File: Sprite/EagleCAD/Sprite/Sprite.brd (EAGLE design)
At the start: 35 x 35 mm, 32 parts, among them P1 SPRITE_PIN, P2 SPRITE_PIN, U1 CC430F5137, U2 HMC5883LSMD, U3 ITG-3200

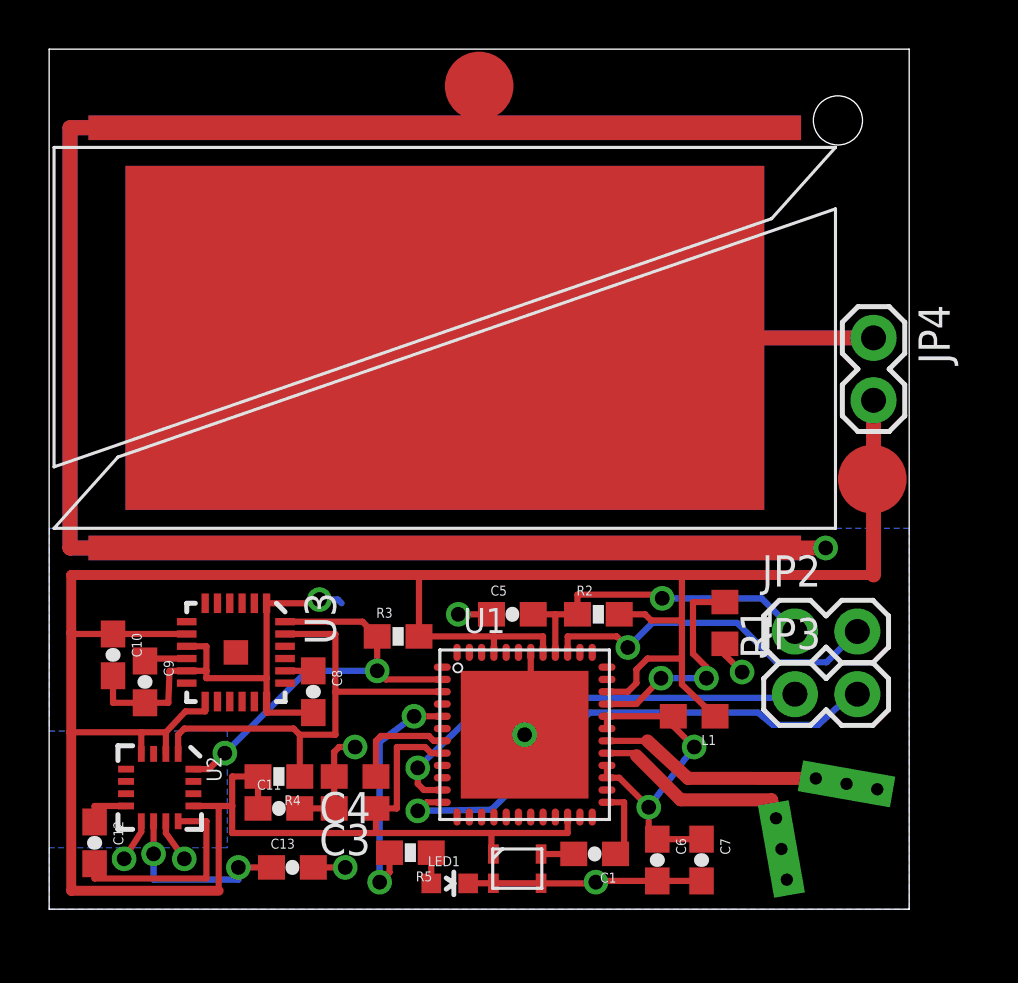
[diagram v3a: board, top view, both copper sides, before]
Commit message: Made corner hole 2.8 mm
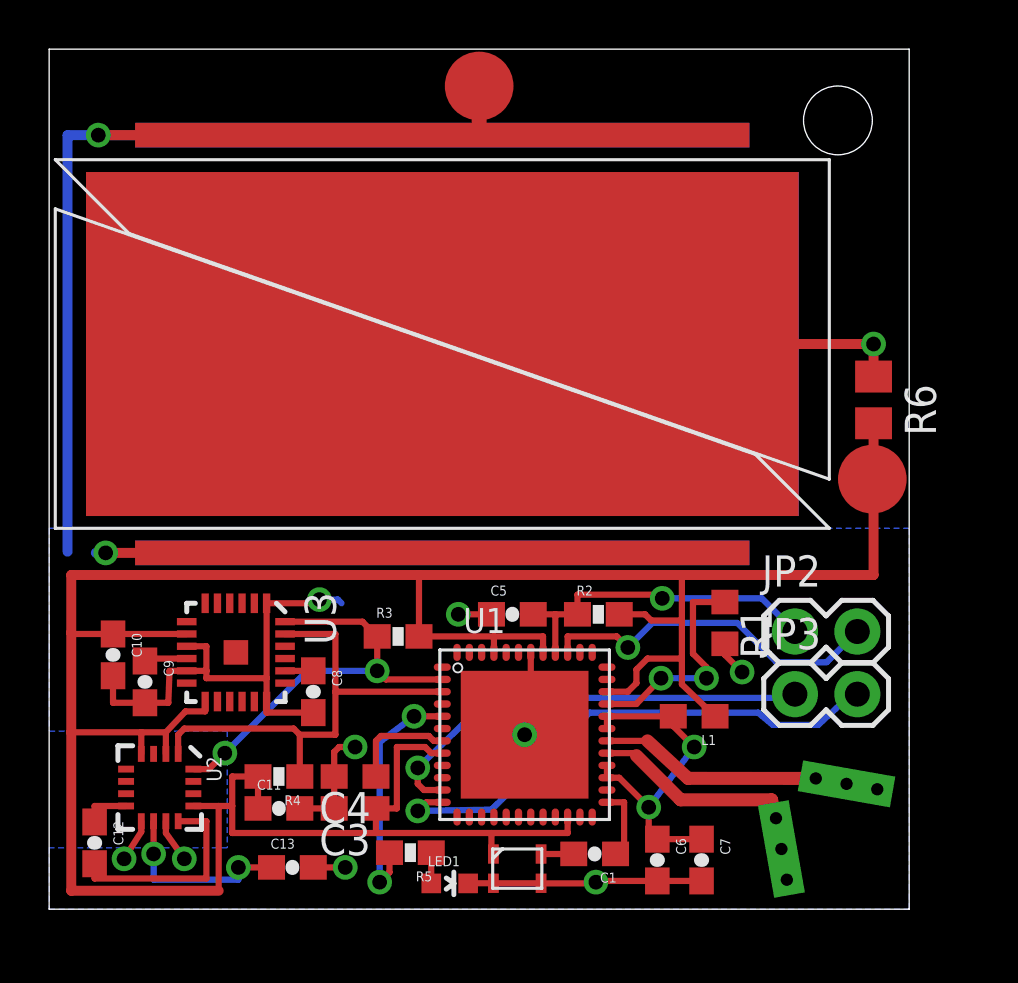
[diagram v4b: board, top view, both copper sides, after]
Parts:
- removed JP4: (no value), SparkFun:1X02
- added R6: 0, rcl:R0805
- moved S2 17.7 mm to (16.0, 23.0)
- moved S1 17.5 mm to (16.0, 23.0)
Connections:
- net VCC: now also R6.2; no longer JP4.2
- net VSOLAR: now also R6.1; no longer JP4.1
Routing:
- net GND: track 156.2 -> 109.3 mm, vias 10 -> 11
- net VSOLAR: track 34.9 -> 36.4 mm, vias 0 -> 1
- net VCC: track 124.2 -> 123.2 mm
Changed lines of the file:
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@@
 <wire x1="35" y1="35" x2="0" y2="35" width="0" layer="20"/>
 <wire x1="0" y1="35" x2="0" y2="0" width="0" layer="20"/>
-<hole x="32.1" y="32.1" drill="2"/>
+<hole x="32.1" y="32.1" drill="2.8"/>
 </plain>
 <attributes>
@@
 <element name="LED1" library="SparkFun" package="LED-0603" value="" x="16.3" y="1.05" rot="R270"/>
 <element name="R5" library="SparkFun" package="0603-RES" value="270R" x="14.7" y="2.3" rot="R180"/>
-<element name="JP4" library="SparkFun" package="1X02" value="" x="33.55" y="23.25" rot="R270"/>
 <element name="JP3" library="SparkFun" package="1X02" value="" x="30.35" y="8.75"/>
-<element name="S2" library="TASC" package="TASC" value="TASC" x="32" y="15.5" rot="MR0"/>
 <element name="U$1" library="SpriteTCXO" package="TXC_7Z" value="TCXO_7Z" x="19.05" y="1.65"/>
 <element name="P2" library="SpritePin" package="SPRITE_PIN" value="SPRITE_PIN" x="17.5" y="33.5"/>
 <element name="P1" library="SpritePin" package="SPRITE_PIN" value="SPRITE_PIN" x="33.5" y="17.5"/>
-<element name="S1" library="TASC" package="TASC" value="TASC" x="0.2" y="15.5"/>
+<element name="S1" library="TASC" package="TASC" value="TASC" x="16" y="23"/>
+<element name="S2" library="TASC" package="TASC" value="TASC" x="16" y="23" rot="MR0"/>
+<element name="R6" library="rcl" package="R0805" value="0" x="33.55" y="20.725" rot="R270"/>
 </elements>
 <signals>
@@
 <wire x1="25.75" y1="9.15" x2="27.1" y2="7.85" width="0.254" layer="1"/>
 <wire x1="24.5" y1="11.75" x2="25.75" y2="11.75" width="0.254" layer="1"/>
-<contactref element="JP4" pad="2"/>
 <contactref element="U$1" pad="VCC"/>
 <wire x1="18.08" y1="2.245" x2="18" y2="2.345" width="0.254" layer="1"/>
 <wire x1="18" y1="2.345" x2="18" y2="3.1" width="0.254" layer="1"/>
-<wire x1="33.55" y1="20.71" x2="33.55" y2="13.6" width="0.6096" layer="1"/>
 <wire x1="25.75" y1="11.75" x2="25.75" y2="13.5" width="0.254" layer="1"/>
 <wire x1="24.5" y1="11.75" x2="24.25" y2="12" width="0.254" layer="1"/>
@@
 <wire x1="6.9" y1="4.2" x2="6.9" y2="0.75" width="0.254" layer="1"/>
 <wire x1="6.9" y1="4.2" x2="5.87" y2="4.2" width="0.254" layer="1"/>
+<contactref element="R6" pad="2"/>
+<wire x1="33.55" y1="19.775" x2="33.55" y2="13.6" width="0.4064" layer="1"/>
 <wire x1="20.1" y1="10.45" x2="22.7" y2="8.85" width="0" layer="19" extent="1-1"/>
 </signal>
@@
 <wire x1="20.02" y1="1.05" x2="20.02" y2="1.055" width="0.254" layer="1"/>
 <wire x1="18.08" y1="1.055" x2="20.02" y2="1.055" width="0.254" layer="1"/>
-<contactref element="S2" pad="MINUS1"/>
-<contactref element="S2" pad="MINUS2"/>
-<contactref element="S1" pad="MINUS2"/>
-<contactref element="S1" pad="MINUS1"/>
-<wire x1="16.1" y1="31.8" x2="0.85" y2="31.8" width="0.6096" layer="16"/>
-<wire x1="0.85" y1="31.8" x2="0.85" y2="14.7" width="0.6096" layer="16"/>
-<wire x1="0.85" y1="14.7" x2="16.1" y2="14.7" width="0.6096" layer="16"/>
-<wire x1="16.1" y1="31.8" x2="0.85" y2="31.8" width="0.6096" layer="1"/>
-<wire x1="0.85" y1="31.8" x2="0.85" y2="14.7" width="0.6096" layer="1"/>
-<wire x1="0.85" y1="14.7" x2="16.1" y2="14.7" width="0.6096" layer="1"/>
 <wire x1="27.5" y1="10.8" x2="27.5" y2="10.35" width="0.254" layer="1"/>
 <wire x1="27.5" y1="10.35" x2="28.2" y2="9.65" width="0.254" layer="1"/>
@@
 <wire x1="10.75" y1="1.7" x2="12.05" y2="1.7" width="0.254" layer="1"/>
 <via x="12.05" y="1.7" extent="1-16" drill="0.6"/>
-<wire x1="16.1" y1="14.7" x2="31.6" y2="14.7" width="0.6096" layer="1"/>
-<via x="31.6" y="14.7" extent="1-16" drill="0.6"/>
-<wire x1="31.6" y1="14.7" x2="31.55" y2="14.7" width="0.6096" layer="16"/>
 <wire x1="20.02" y1="1.05" x2="22.2" y2="1.05" width="0.254" layer="1"/>
 <wire x1="22.2" y1="1.05" x2="22.25" y2="1.1" width="0.254" layer="1"/>
@@
 <vertex x="0" y="2.5"/>
 </polygon>
+<contactref element="S1" pad="MINUS1"/>
+<contactref element="S1" pad="MINUS2"/>
+<contactref element="S2" pad="MINUS1"/>
+<contactref element="S2" pad="MINUS2"/>
+<wire x1="16" y1="31.5" x2="17.5" y2="31.5" width="0.4064" layer="1"/>
+<wire x1="17.5" y1="31.5" x2="17.5" y2="33.5" width="0.6096" layer="1"/>
+<wire x1="16" y1="31.5" x2="2" y2="31.5" width="0.4064" layer="1"/>
+<wire x1="16" y1="14.55" x2="16" y2="14.5" width="0.4064" layer="1"/>
+<wire x1="16" y1="31.5" x2="2" y2="31.5" width="0.4064" layer="16"/>
+<via x="2" y="31.5" extent="1-16" drill="0.6"/>
+<wire x1="2" y1="31.5" x2="0.75" y2="31.5" width="0.4064" layer="16"/>
+<wire x1="0.75" y1="31.5" x2="0.75" y2="14.55" width="0.4064" layer="16"/>
+<wire x1="16" y1="14.5" x2="2.3" y2="14.5" width="0.4064" layer="1"/>
+<via x="2.3" y="14.5" extent="1-16" drill="0.6"/>
+<wire x1="2.3" y1="14.5" x2="1.9" y2="14.5" width="0.4064" layer="16"/>
 </signal>
 <signal name="N$3">
@@
 </signal>
 <signal name="VSOLAR">
-<contactref element="JP4" pad="1"/>
+<contactref element="S1" pad="PLUS"/>
 <contactref element="S2" pad="PLUS"/>
-<contactref element="S1" pad="PLUS"/>
-<wire x1="33.55" y1="23.25" x2="16.1" y2="23.25" width="0.6096" layer="1"/>
-<wire x1="16.1" y1="23.25" x2="33.55" y2="23.25" width="0.6096" layer="16"/>
+<contactref element="R6" pad="1"/>
+<wire x1="16" y1="23" x2="33.55" y2="23" width="0.4064" layer="1"/>
+<wire x1="16" y1="23" x2="33.55" y2="23" width="0.4064" layer="16"/>
+<via x="33.55" y="23" extent="1-16" drill="0.6"/>
+<wire x1="33.55" y1="23" x2="33.55" y2="21.675" width="0.4064" layer="1"/>
 </signal>
 <signal name="TXD">
@@
 </signal>
 </signals>
-<errors>
-</errors>
 </board>
 </drawing>

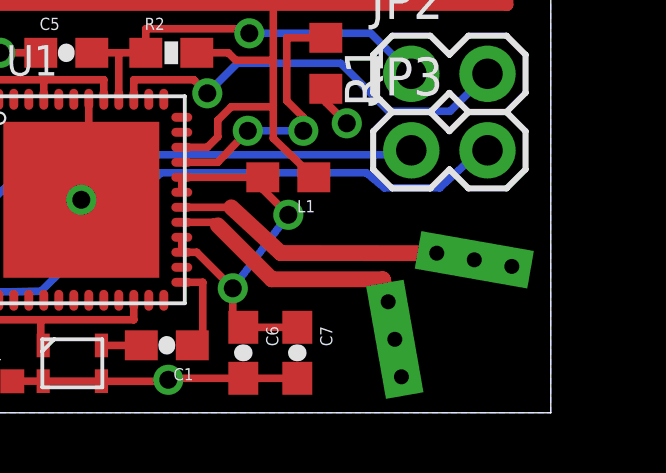
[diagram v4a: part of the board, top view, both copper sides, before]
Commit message: Updated Gerbers and BOM for new Sprite order
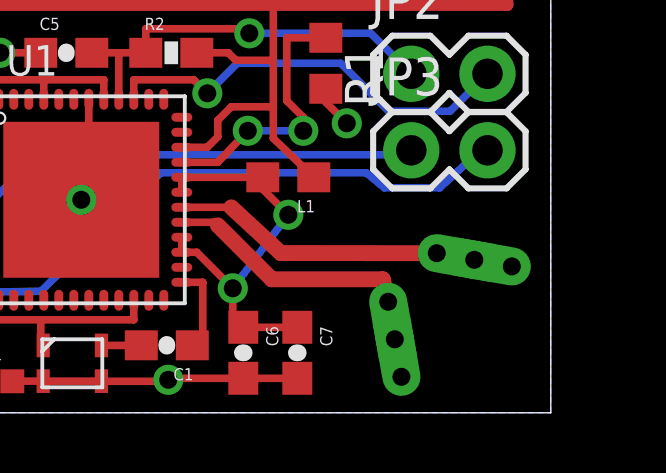
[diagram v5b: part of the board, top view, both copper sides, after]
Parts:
- renumbered U$1 to X1
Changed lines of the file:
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@@
 <element name="R5" library="SparkFun" package="0603-RES" value="270R" x="14.7" y="2.3" rot="R180"/>
 <element name="JP3" library="SparkFun" package="1X02" value="" x="30.35" y="8.75"/>
-<element name="U$1" library="SpriteTCXO" package="TXC_7Z" value="TCXO_7Z" x="19.05" y="1.65"/>
+<element name="X1" library="SpriteTCXO" package="TXC_7Z" value="TCXO_7Z" x="19.05" y="1.65"/>
 <element name="P2" library="SpritePin" package="SPRITE_PIN" value="SPRITE_PIN" x="17.5" y="33.5"/>
 <element name="P1" library="SpritePin" package="SPRITE_PIN" value="SPRITE_PIN" x="33.5" y="17.5"/>
@@
 <wire x1="25.75" y1="9.15" x2="27.1" y2="7.85" width="0.254" layer="1"/>
 <wire x1="24.5" y1="11.75" x2="25.75" y2="11.75" width="0.254" layer="1"/>
-<contactref element="U$1" pad="VCC"/>
+<contactref element="X1" pad="VCC"/>
 <wire x1="18.08" y1="2.245" x2="18" y2="2.345" width="0.254" layer="1"/>
 <wire x1="18" y1="2.345" x2="18" y2="3.1" width="0.254" layer="1"/>
@@
 <wire x1="6.4" y1="9.7" x2="5.6" y2="9.7" width="0.254" layer="1"/>
 <wire x1="6.4" y1="9.7" x2="6.4" y2="9.4" width="0.254" layer="1"/>
-<contactref element="U$1" pad="GND2"/>
-<contactref element="U$1" pad="GND1"/>
+<contactref element="X1" pad="GND2"/>
+<contactref element="X1" pad="GND1"/>
 <wire x1="20.02" y1="1.05" x2="20.02" y2="1.055" width="0.254" layer="1"/>
 <wire x1="18.08" y1="1.055" x2="20.02" y2="1.055" width="0.254" layer="1"/>
@@
 <contactref element="ANT-N" pad="IN3"/>
 <contactref element="ANT-N" pad="IN2"/>
-<wire x1="32.45" y1="5.1" x2="33.700703125" y2="4.879465625" width="0.53" layer="1"/>
-<wire x1="31.19929375" y1="5.32053125" x2="32.45" y2="5.1" width="0.53" layer="1"/>
+<wire x1="31.19929375" y1="5.32053125" x2="33.700703125" y2="4.879465625" width="0.53" layer="1"/>
 <wire x1="26" y1="5.325" x2="31.19929375" y2="5.32053125" width="0.53" layer="1"/>
 <wire x1="22.7" y1="6.85" x2="24.35" y2="6.85" width="0.254" layer="1"/>
 <wire x1="24.35" y1="6.85" x2="26" y2="5.325" width="0.53" layer="1"/>
+<wire x1="33.700703125" y1="4.879465625" x2="32.45" y2="5.1" width="0" layer="19" extent="1-1"/>
 </signal>
 <signal name="RFP">
@@
 <contactref element="ANT-P" pad="IN3"/>
 <contactref element="ANT-P" pad="IN2"/>
-<wire x1="30.02053125" y1="1.19929375" x2="29.8" y2="2.45" width="0.53" layer="1"/>
+<wire x1="30.02053125" y1="1.19929375" x2="29.579465625" y2="3.700703125" width="0.53" layer="1"/>
 <wire x1="23.9" y1="6.25" x2="25.7" y2="4.45" width="0.53" layer="1"/>
 <wire x1="25.7" y1="4.45" x2="29.4" y2="4.45" width="0.53" layer="1"/>
 <wire x1="22.7" y1="6.35" x2="23.75" y2="6.35" width="0.254" layer="1"/>
 <wire x1="23.75" y1="6.35" x2="23.9" y2="6.25" width="0.254" layer="1"/>
-<wire x1="29.8" y1="2.45" x2="29.579465625" y2="3.700703125" width="0.53" layer="1"/>
 <wire x1="29.579465625" y1="3.700703125" x2="29.4" y2="4.45" width="0.53" layer="1"/>
+<wire x1="30.02053125" y1="1.19929375" x2="29.8" y2="2.45" width="0" layer="19" extent="1-1"/>
 </signal>
 <signal name="RST">
@@
 <signal name="N$12">
 <contactref element="C1" pad="2"/>
-<contactref element="U$1" pad="OUT"/>
+<contactref element="X1" pad="OUT"/>
 <wire x1="20.02" y1="2.245" x2="21.15" y2="2.245" width="0.254" layer="1"/>
 <wire x1="21.15" y1="2.245" x2="21.35" y2="2.25" width="0.254" layer="1"/>
@@
 </signal>
 </signals>
+<errors>
+</errors>
 </board>
 </drawing>

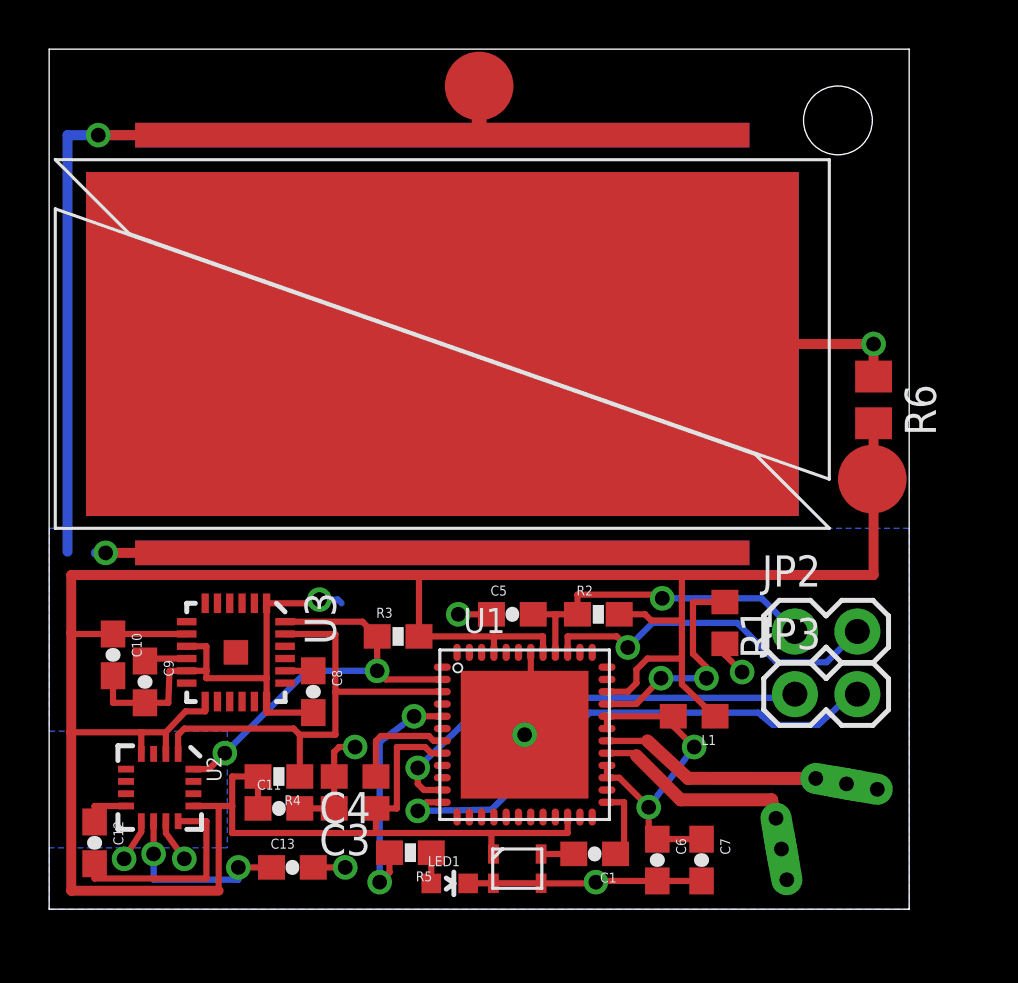
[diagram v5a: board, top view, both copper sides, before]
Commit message: Fixed silksreen on Sprite board
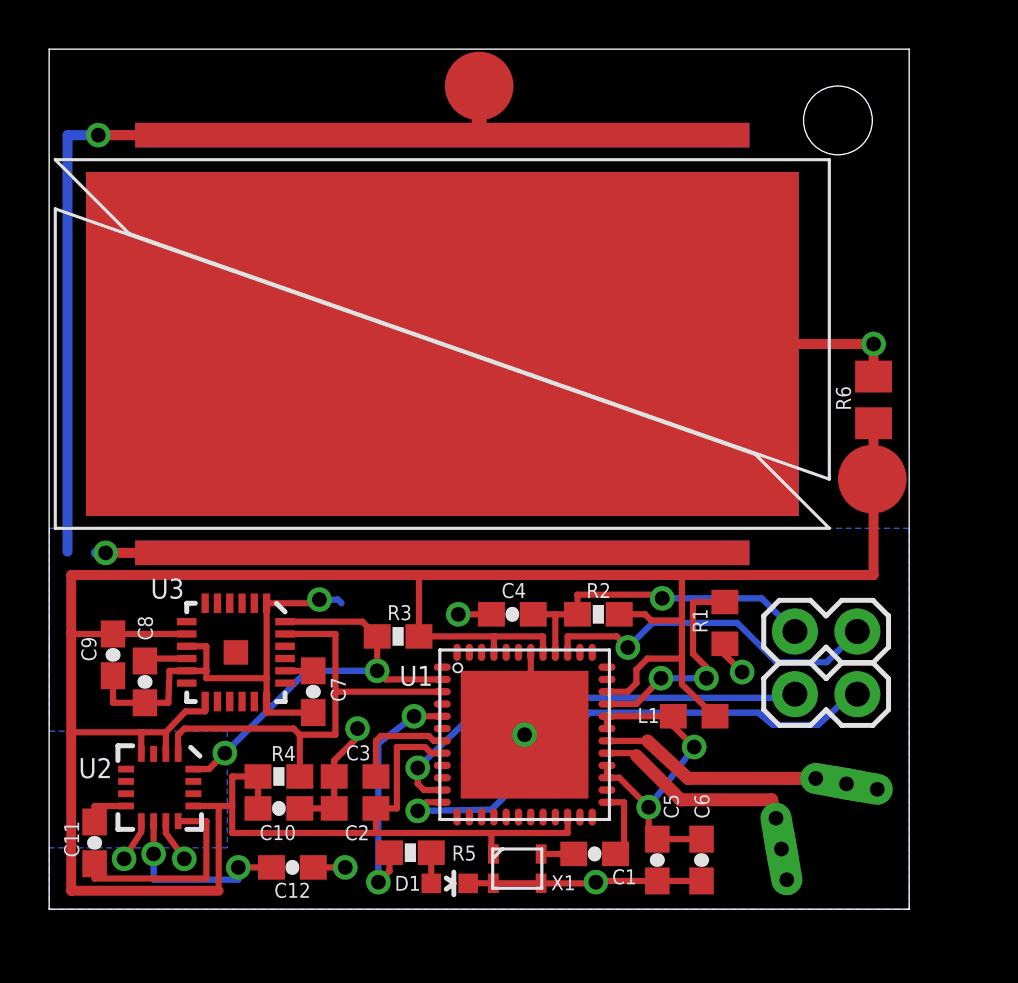
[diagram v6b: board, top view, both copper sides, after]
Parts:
- removed C13: 4.7uF, SparkFun:0603-CAP
- added C2: 470nF, rcl:C0603
- C10, C6: value 10nF -> 100nF
- C11: value 100nF -> 220nF
- C12: value 220nF -> 4.7uF
- C4: value 470nF -> 2.2nF; device rcl:C0603 -> SparkFun:0603-CAP
- C5: value 2.2nF -> 10nF
- C7: value 100nF -> 2.2nF
- C8: value 2.2nF -> 100nF
- C9: value 100nF -> 10nF
- moved C7 17.2 mm to (10.8, 8.85)
- moved C5 11.6 mm to (24.8, 2.00), turned to 270 degrees
- moved C10 9.20 mm to (9.35, 4.10), turned to 0 degrees
- moved C4 9.19 mm to (18.9, 12.0), turned to 0 degrees
- moved C12 8.11 mm to (9.90, 1.70), turned to 0 degrees
- moved C11 7.63 mm to (1.85, 2.70), turned to 270 degrees
- moved C8 6.86 mm to (3.90, 9.25)
- moved C6 1.80 mm to (26.6, 2.00)
- moved C9 1.70 mm to (2.60, 10.3)
- moved C3 1.30 mm to (12.4, 5.40)
- renumbered LED1 to D1
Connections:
- net GND: now also C12.2, C2.2, C4.1, C5.2; no longer C11.2, C13.2, C4.2, C5.1
- net N$4: now also C3.1; no longer C4.1
- net N$5: now also C11.1; no longer C12.1
- net N$6: now also C11.2; no longer C12.2
- net N$7: now also C12.1; no longer C13.1
- net N$8: now also C7.1; no longer C8.1
- net N$9: now also C8.1; no longer C9.1
- net RST: now also C4.2; no longer C5.2
- net VCC: now also C2.1, C9.1; no longer C11.1, C3.1
- net VCCRF: now also C5.1; no longer C7.1
